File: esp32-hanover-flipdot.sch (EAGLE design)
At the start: 28 parts, among them J1 DC-005, J2 HANOVER, J3 FTDI, Q1 NCE3407A, Q2 S9013, U1 ESP32-PICO-D4, U2 CJA1117B-3.3-SOT89, U3 LM2576SX-5.0/NOPB

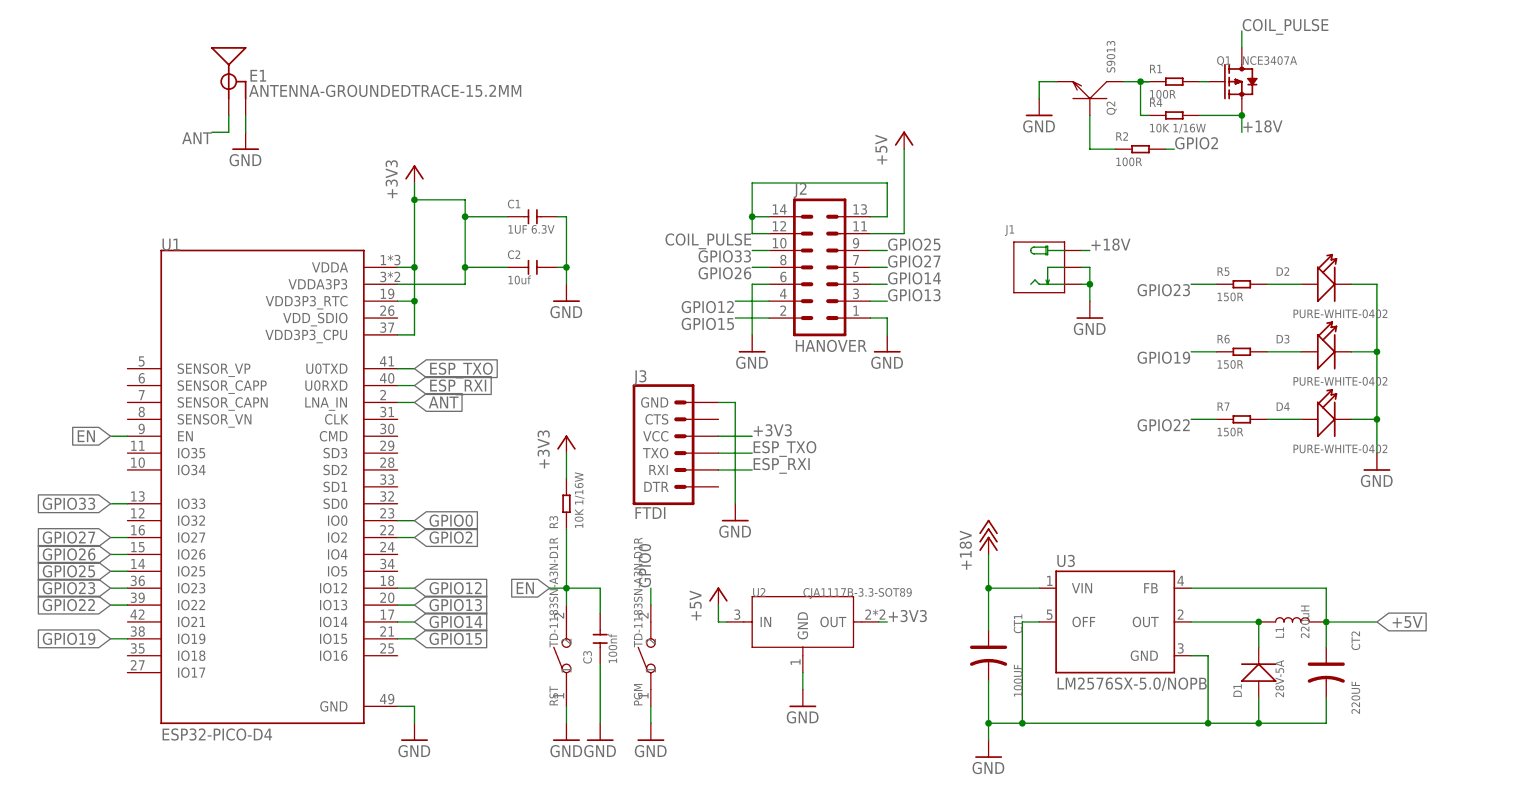
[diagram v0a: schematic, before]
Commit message: Change buck converter from LM7576-5.0 to AP63205, change antenna
Change buck converter from LM7576-5.0 to AP63205, which uses drastically less space and switches at a higher frequency thus requiring smaller passives, and does not require a schottky diode.

Change antenna to a larger inverted-F antenna which has more isotropic gain thus makes placement of the board less of a factor in Wi-Fi performance.
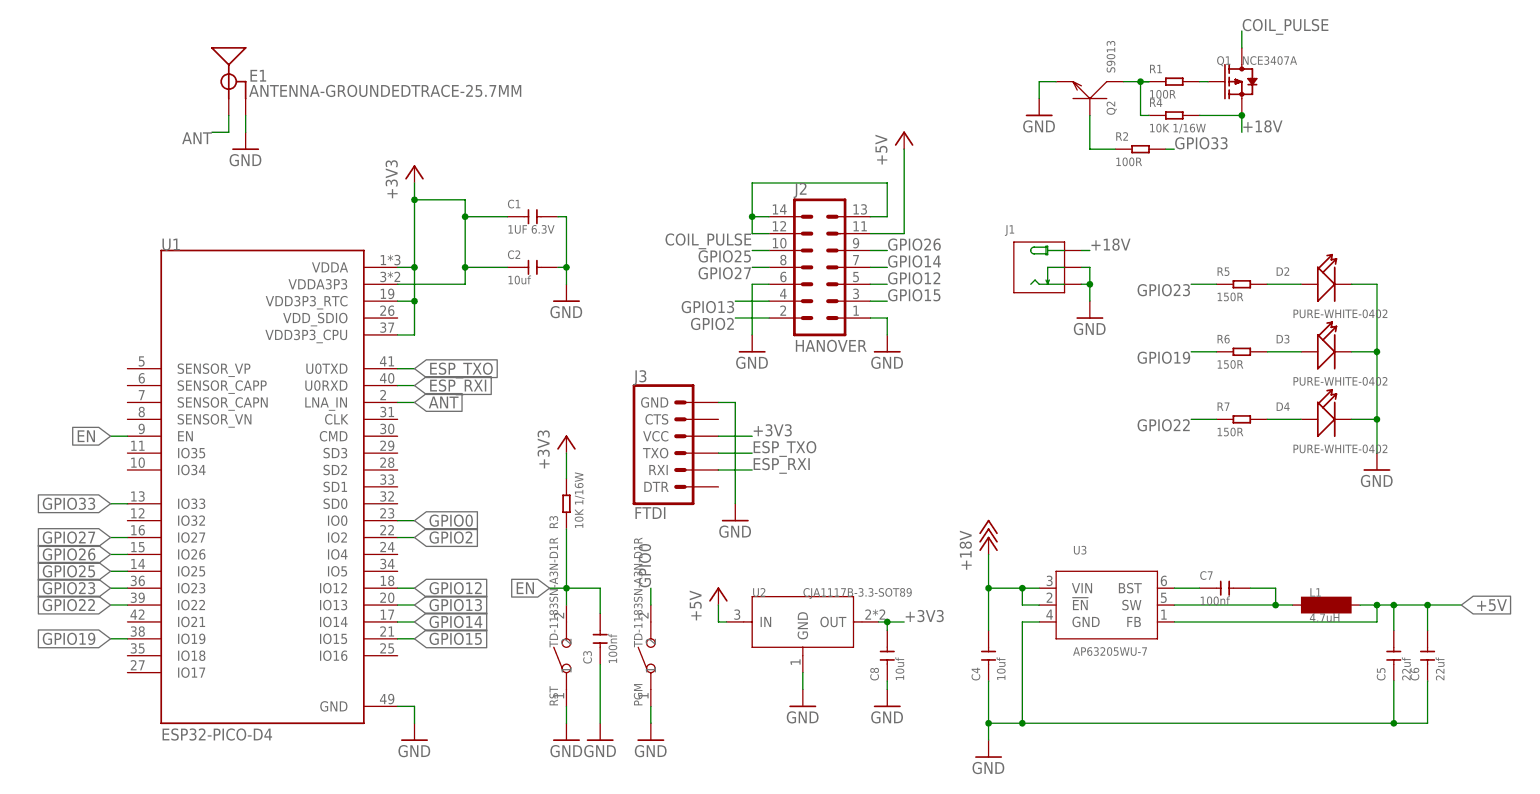
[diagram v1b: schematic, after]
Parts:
- removed CT1: 100UF, OPL_Capacitor:ALUMINUM-SMD-220UF-16V(D6.3-H7.7MM)
- removed CT2: 220UF, OPL_Capacitor:ALUMINUM-SMD-220UF-16V(D6.3-H7.7MM)
- removed D1: 28V-5A, OPL_Discrete_Semiconductor:SMD-DIODE-SCHOTTKY-28V-5A(DO-214AA)
- added C4: 10uf, OPL_Capacitor_No_Thermals:CERAMIC-10UF-25V-10%-X5R(0805)
- added C5, C6: 22uf, OPL_Capacitor_No_Thermals:CERAMIC-22UF-6.3V-20%-X5R(0805)
- added C7: 100nf, OPL_Capacitor:CERAMIC-100NF-25V-10%-X7R(0402)
- added C8: 10uf, OPL_Capacitor:CERAMIC-10UF-6.3V-20%-X5R(0402)
- E1: value ANTENNA-GROUNDEDTRACE-15.2MM -> ANTENNA-GROUNDEDTRACE-25.7MM; device SparkFun-RF:ANTENNA-GROUNDEDTRACE-15.2MM -> SparkFun-RF-GND-Extended:ANTENNA-GROUNDEDTRACE-25.7MM
- L1: value 220uH -> 4.7uH; device SparkFun-Coils:INDUCTOR-CR54-3.3UH -> TDK VLS201610HBX-1:VLS201610HBX-4R7M-1
- U3: value LM2576SX-5.0/NOPB -> AP63205WU-7; device LM2576 (1):LM2576S -> Diodes_Inc_AP6320:AP63205WU-7
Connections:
- new net N$8: C7.2, L1.1, U3.SW
- net +18V: now also C4.2, U3.!EN; no longer CT1.+
- net +3V3: now also C8.2
- net +5V: now also C5.2, C6.2; no longer CT2.+
- net GND: now also C4.1, C5.1, C6.1, C8.1; no longer CT1.-, CT2.-, D1.+, U3.OFF
- net GPIO12: now also J2.5; no longer J2.4
- net GPIO13: now also J2.4; no longer J2.3
- net GPIO14: now also J2.7; no longer J2.5
- net GPIO15: now also J2.3; no longer J2.2
- net GPIO2: now also J2.2; no longer R2.2
- net GPIO25: now also J2.10; no longer J2.9
- net GPIO26: now also J2.9; no longer J2.8
- net GPIO27: now also J2.8; no longer J2.7
- net GPIO33: now also R2.2; no longer J2.10
- net N$4: now also C7.1, U3.BST; no longer D1.-, L1.1, U3.OUT
